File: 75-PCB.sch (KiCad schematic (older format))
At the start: 322 parts, among them J1 AVR-ISP-6, SW1 SW_Push, U1 AT90USB1286-AU, U2 PRTR5V0U2X, Y1 16MHz

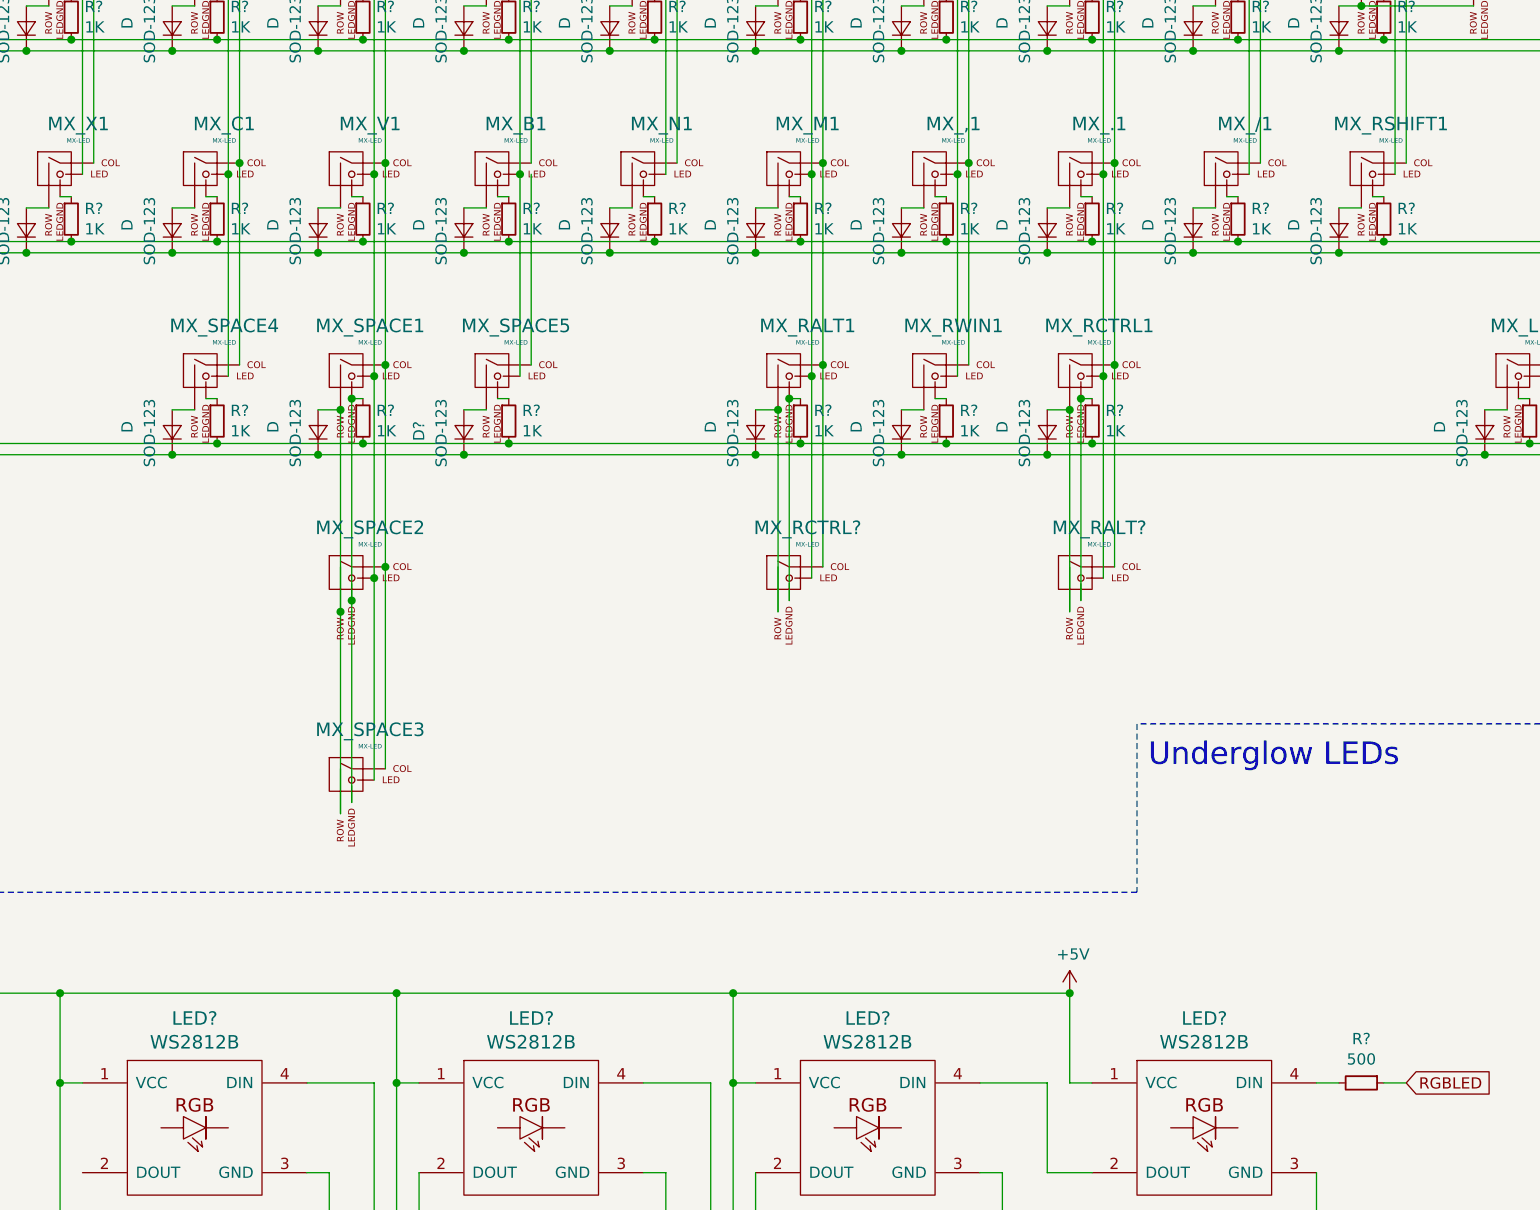
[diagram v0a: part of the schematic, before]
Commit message: Added switches for JIS bottom row
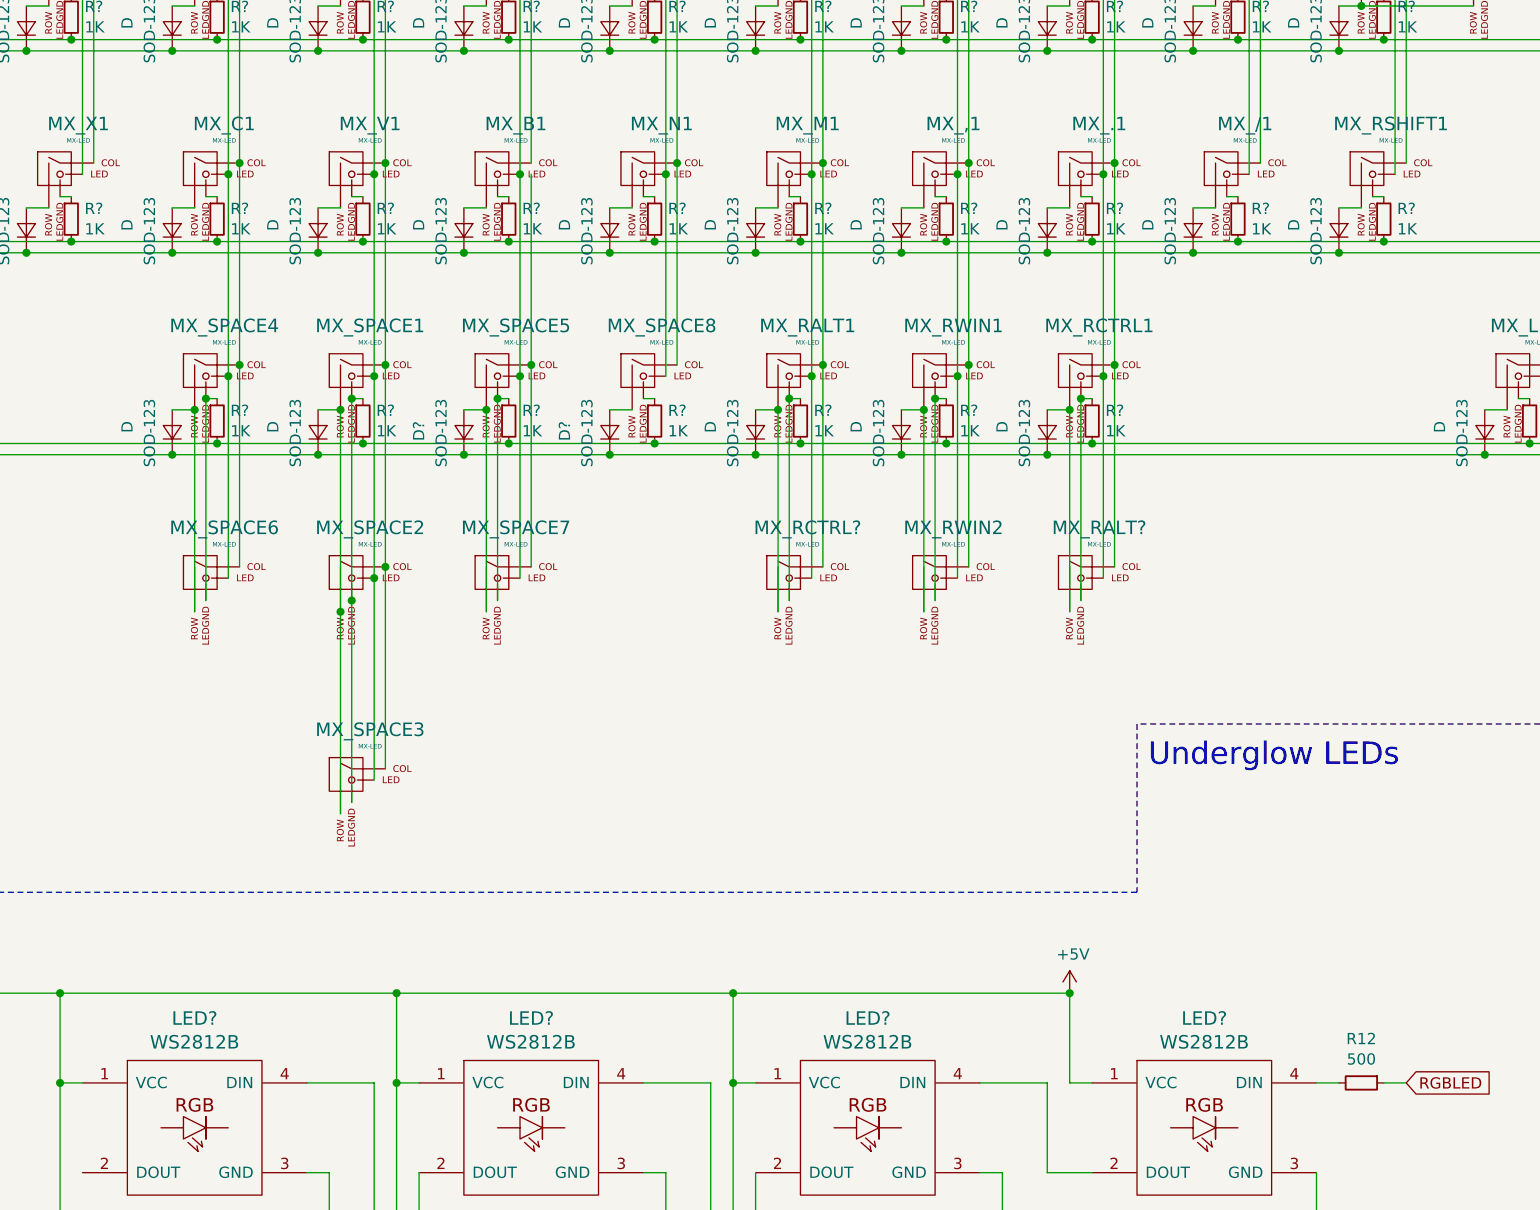
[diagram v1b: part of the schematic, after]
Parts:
- added D?: SOD-123, symbol Device:D_Small
- added MX_RWIN2, MX_SPACE6, MX_SPACE7, MX_SPACE8: MX-LED, symbol MX_Alps_Hybrid:MX-LED
- added R?: 1K, symbol Device:R_Small
- gave numbers to parts that had none: 1
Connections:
- net +5V: now also MX_RWIN2.3 (LED), MX_SPACE6.3 (LED), MX_SPACE7.3 (LED), MX_SPACE8.3 (LED)
- net COL4: now also MX_SPACE6.1 (COL)
- net COL7: now also MX_SPACE8.1 (COL)
- net COL9: now also MX_RWIN2.1 (COL)
- net LEDGND: now also R?.2
- net ROW5: now also D?.1 (K)
- net at D.2 (A), MX_SPACE4.2 (ROW): now also MX_SPACE6.2 (ROW)
- net at MX_SPACE4.4 (LEDGND), R?.1: now also MX_SPACE6.4 (LEDGND)
- net at MX_SPACE5.1 (COL): now also MX_SPACE7.1 (COL)
- net at D?.2 (A), MX_SPACE5.2 (ROW): now also MX_SPACE7.2 (ROW)
- net at MX_SPACE5.4 (LEDGND), R?.1: now also MX_SPACE7.4 (LEDGND)
- net at D.2 (A), MX_RWIN1.2 (ROW): now also MX_RWIN2.2 (ROW)
- net at MX_RWIN1.4 (LEDGND), R?.1: now also MX_RWIN2.4 (LEDGND)
- new net: D?.2 (A), MX_SPACE8.2 (ROW)
- new net: MX_SPACE8.4 (LEDGND), R?.1
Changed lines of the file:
@@
 Connection ~ 6300 6300
 Wire Wire Line
-	6300 6300 5000 6300
+	6300 6300 5650 6300
 Connection ~ 6950 6300
 Wire Wire Line
@@
 Connection ~ 6500 6250
 Wire Wire Line
-	6500 6250 5200 6250
+	6500 6250 5850 6250
 Connection ~ 7150 6250
 Wire Wire Line
@@
 Underglow LEDs
 $Comp
-L Device:R_Small R?
+L Device:R_Small R12
 U 1 1 62B9EC55
 P 9000 9100
-F 0 "R?" V 8804 9100 50  0000 C CNN
+F 0 "R12" V 8804 9100 50  0000 C CNN
 F 1 "500" V 8895 9100 50  0000 C CNN
 F 2 "" H 9000 9100 50  0001 C CNN
@@
 Wire Wire Line
 	9100 9100 9200 9100
+$Comp
+L MX_Alps_Hybrid:MX-LED MX_SPACE6
+U 1 1 5E97F791
+P 3850 6850
+F 0 "MX_SPACE6" H 3932 7074 60  0000 C CNN
+F 1 "MX-LED" H 3932 7000 20  0000 C CNN
+F 2 "" H 3225 6825 60  0001 C CNN
+F 3 "" H 3225 6825 60  0001 C CNN
+	1    3850 6850
+	1    0    0    -1
+$EndComp
+Wire Wire Line
+	3800 7000 3800 6100
+Connection ~ 3800 6100
+Wire Wire Line
+	3850 6950 3850 6050
+Connection ~ 3850 6050
+Wire Wire Line
+	3950 6850 3950 5950
+Connection ~ 3950 5950
+Wire Wire Line
+	4000 6800 4000 5900
+Connection ~ 4000 5900
+$Comp
+L MX_Alps_Hybrid:MX-LED MX_SPACE7
+U 1 1 5ED76FE4
+P 5150 6850
+F 0 "MX_SPACE7" H 5232 7074 60  0000 C CNN
+F 1 "MX-LED" H 5232 7000 20  0000 C CNN
+F 2 "" H 4525 6825 60  0001 C CNN
+F 3 "" H 4525 6825 60  0001 C CNN
+	1    5150 6850
+	1    0    0    -1
+$EndComp
+Wire Wire Line
+	5100 7000 5100 6100
+Connection ~ 5100 6100
+Wire Wire Line
+	5150 6950 5150 6050
+Connection ~ 5150 6050
+Wire Wire Line
+	5250 6850 5250 5950
+Connection ~ 5250 5950
+Wire Wire Line
+	5300 6800 5300 5900
+Connection ~ 5300 5900
+$Comp
+L MX_Alps_Hybrid:MX-LED MX_RWIN2
+U 1 1 5F179ACB
+P 7100 6850
+F 0 "MX_RWIN2" H 7182 7074 60  0000 C CNN
+F 1 "MX-LED" H 7182 7000 20  0000 C CNN
+F 2 "" H 6475 6825 60  0001 C CNN
+F 3 "" H 6475 6825 60  0001 C CNN
+	1    7100 6850
+	1    0    0    -1
+$EndComp
+Wire Wire Line
+	7050 7000 7050 6100
+Connection ~ 7050 6100
+Wire Wire Line
+	7100 6950 7100 6050
+Connection ~ 7100 6050
+Wire Wire Line
+	7200 6850 7200 5950
+Connection ~ 7200 5950
+Wire Wire Line
+	7250 6800 7250 5900
+Connection ~ 7250 5900
+$Comp
+L MX_Alps_Hybrid:MX-LED MX_SPACE8
+U 1 1 5F57F0CF
+P 5800 5950
+F 0 "MX_SPACE8" H 5882 6174 60  0000 C CNN
+F 1 "MX-LED" H 5882 6100 20  0000 C CNN
+F 2 "" H 5175 5925 60  0001 C CNN
+F 3 "" H 5175 5925 60  0001 C CNN
+	1    5800 5950
+	1    0    0    -1
+$EndComp
+Wire Wire Line
+	5950 5900 5950 5000
+Connection ~ 5950 5000
+Wire Wire Line
+	5900 5050 5900 5950
+Connection ~ 5900 5050
+$Comp
+L Device:D_Small D?
+U 1 1 5F7EF6F4
+P 5650 6200
+F 0 "D?" H 5700 6400 50  0000 R CNN
+F 1 "SOD-123" H 5800 6300 50  0000 R CNN
+F 2 "" V 5650 6200 50  0001 C CNN
+F 3 "~" V 5650 6200 50  0001 C CNN
+	1    5650 6200
+	0    -1   -1   0
+$EndComp
+Wire Wire Line
+	5650 6100 5750 6100
+Connection ~ 5650 6300
+Wire Wire Line
+	5650 6300 5000 6300
+$Comp
+L Device:R_Small R?
+U 1 1 5F99E7F5
+P 5850 6150
+F 0 "R?" H 5909 6196 50  0000 L CNN
+F 1 "1K" H 5909 6105 50  0000 L CNN
+F 2 "" H 5850 6150 50  0001 C CNN
+F 3 "~" H 5850 6150 50  0001 C CNN
+	1    5850 6150
+	1    0    0    -1
+$EndComp
+Connection ~ 5850 6250
+Wire Wire Line
+	5850 6250 5200 6250
+Wire Wire Line
+	5800 6050 5850 6050
 $EndSCHEMATC

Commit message: Assigned footprints
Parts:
- removed D?: SOD-123, symbol Device:D_Small
- removed MX_RWIN2, MX_SPACE6, MX_SPACE7, MX_SPACE8: MX-LED, symbol MX_Alps_Hybrid:MX-LED
- removed R?: 1K, symbol Device:R_Small
- added MX_BCKSP2: MX-LED, MX_Only:MXOnly-1U, symbol MX_Alps_Hybrid:MX-LED
- added MX_CAPS2: MX-LED, MX_Only:MXOnly-1.25U, symbol MX_Alps_Hybrid:MX-LED
- C1, C2, C3, C4, C5, C6, C7: footprint (none) -> Capacitor_SMD:C_0805_2012Metric
- C10, C11, C12, C13, C14, C15, C16, C8, C9: renamed from C?; footprint (none) -> Capacitor_SMD:C_0805_2012Metric
- D1: footprint (none) -> random-keyboard-parts:D_SOD-123-Pretty
- D10, D11, D12, D13, D14, D15, D16, D17, D18, D19, D2, D20, D21, D22, D23, D24, D25, D26, D27, D28, D29, D3, D30, D31, D32, D33, D34, D35, D36, D37, D38, D39, D4, D40, D41, D43, D44, D45, D46, D47, D48, D49, D5, D50, D51, D52, D53, D54, D55, D56, D57, D58, D59, D6, D60, D61, D62, D63, D64, D65, D66, D67, D68, D69, D7, D70, D71, D72, D73, D74, D75, D76, D77, D78, D79, D8, D80, D81, D82, D83, D84, D85, D89, D9, D90, D91: renamed from D; footprint (none) -> random-keyboard-parts:D_SOD-123-Pretty
- D42: renamed from D?; footprint (none) -> random-keyboard-parts:D_SOD-123-Pretty
- D86, D87, D88: footprint (none) -> random-keyboard-parts:LED_D3.0mm-Pretty
- F1: footprint (none) -> Fuse:Fuse_1206_3216Metric
- LED1, LED2, LED3, LED4, LED5, LED6, LED7, LED8, LED9: renamed from LED?; footprint (none) -> WS2812B:WS2812B
- MX_#1, MX_#10, MX_#2, MX_#3, MX_#4, MX_#5, MX_#6, MX_#7, MX_#8, MX_#9, MX_'1, MX_,1, MX_-1, MX_.1, MX_/1, MX_;1, MX_=1, MX_A1, MX_B1, MX_C1, MX_D1, MX_DEL1, MX_DOWN1, MX_E1, MX_END1, MX_ESC1, MX_F#1, MX_F#10, MX_F#11, MX_F#12, MX_F#2, MX_F#3, MX_F#4, MX_F#5, MX_F#6, MX_F#7, MX_F#8, MX_F#9, MX_F1, MX_G1, MX_H1, MX_HOME1, MX_I1, MX_J1, MX_K1, MX_L1, MX_LEFT1, MX_LSHIFT3, MX_LWIN2, MX_M1, MX_N1, MX_O1, MX_P1, MX_PAUSE1, MX_PGDN1, MX_PGUP1, MX_Q1, MX_R1, MX_RALT1, MX_RCTRL1, MX_RIGHT1, MX_RWIN1, MX_S1, MX_T1, MX_U1, MX_UP1, MX_V1, MX_W1, MX_X1, MX_Y1, MX_Z1, MX_[1, MX_\2, MX_]1, MX_`1: footprint (none) -> MX_Only:MXOnly-1U
- MX_BCKSP1: footprint (none) -> MX_Only:MXOnly-2U
- MX_BCKSP3: renamed from MX_BCKSP2; footprint (none) -> MX_Only:MXOnly-1U
- MX_CAPS1, MX_RSHIFT1: footprint (none) -> MX_Only:MXOnly-1.75U
- MX_ENTER1, MX_SPACE5: footprint (none) -> MX_Only:MXOnly-2.25U-ReversedStabilizers
- MX_ENTER2: footprint (none) -> MX_Only:MXOnly-ISO-ReversedStabilizers
- MX_LALT1, MX_LCTRL1, MX_LSHIFT2, MX_LWIN1, MX_SPACE3: footprint (none) -> MX_Only:MXOnly-1.25U
- MX_LALT2, MX_LCTRL2, MX_TAB1, MX_\1: footprint (none) -> MX_Only:MXOnly-1.5U
- MX_LALT3: renamed from MX_LALT?; footprint (none) -> MX_Only:MXOnly-1.5U
- MX_LCTRL3: renamed from MX_LCTRL?; footprint (none) -> MX_Only:MXOnly-1.5U
- MX_LSHIFT1: footprint (none) -> MX_Only:MXOnly-2.25U
- MX_RALT2: renamed from MX_RALT?; footprint (none) -> MX_Only:MXOnly-1.5U
- MX_RCTRL2: renamed from MX_RCTRL?; footprint (none) -> MX_Only:MXOnly-1.5U
- MX_SPACE1: footprint (none) -> MX_Only:MXOnly-6.25U-ReversedStabilizers
- MX_SPACE2: footprint (none) -> MX_Only:MXOnly-7U-ReversedStabilizers
- MX_SPACE4: footprint (none) -> MX_Only:MXOnly-2.75U-ReversedStabilizers
- R1, R10, R11, R12, R2, R3, R4, R5, R6, R7, R8, R9: footprint (none) -> Resistor_SMD:R_0805_2012Metric
- R13, R14, R15, R16, R17, R18, R19, R20, R21, R22, R23, R24, R25, R26, R27, R28, R29, R30, R31, R32, R33, R34, R35, R36, R37, R38, R39, R40, R41, R42, R43, R44, R45, R46, R47, R48, R49, R50, R51, R52, R53, R54, R55, R56, R57, R58, R59, R60, R61, R62, R63, R64, R65, R66, R67, R68, R69, R70, R71, R72, R73, R74, R75, R76, R77, R78, R79, R80, R81, R82, R83, R84, R85, R86, R87, R88, R89, R90, R91, R92, R93, R94, R95, R96, R97, R98, R99: renamed from R?; footprint (none) -> Resistor_SMD:R_0805_2012Metric
- SW1: footprint (none) -> random-keyboard-parts:SKQG-1155865
- U2: footprint (none) -> random-keyboard-parts:SOT143B
- Y1: footprint (none) -> Crystal:Crystal_SMD_3225-4Pin_3.2x2.5mm
- gave numbers to parts that had none: 1
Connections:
- net +5V: now also MX_BCKSP2.3 (LED), MX_CAPS2.3 (LED)
- net COL0: now also MX_CAPS2.1 (COL)
- net COL13: now also MX_BCKSP2.1 (COL)
- net at D77.2 (A), MX_BCKSP1.2 (ROW): now also MX_BCKSP2.2 (ROW)
- net at D5.2 (A), MX_CAPS1.2 (ROW): now also MX_CAPS2.2 (ROW)
- net at MX_BCKSP1.4 (LEDGND), R88.1: now also MX_BCKSP2.4 (LEDGND)
- net at MX_CAPS1.4 (LEDGND), R16.1: now also MX_CAPS2.4 (LEDGND)
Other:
- moved on the sheet: LED1, LED2, LED3, LED4, LED5, LED6, LED7, LED8, LED9, MX_SPACE3, R12
